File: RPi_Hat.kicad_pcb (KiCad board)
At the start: 2 copper layers, 65 x 56 mm, 50 parts, among them J1 Conn_01x02_Male, J2 RPi_GPIO, J3 Conn_02x03_Counter_Clockwise, J5 Conn_01x03_Male, J6 Conn_01x03_Male, J7 Conn_01x03_Male, J8 Conn_01x03_Male, J9 Conn_01x03_Male, SW1 SW_Push, U1 LM1085-5.0, U2 STM32F030CCTx, U3 MAX485E, U4 MAX485E, U5 MAX485E, U6 MAX485E, U7 MAX485E

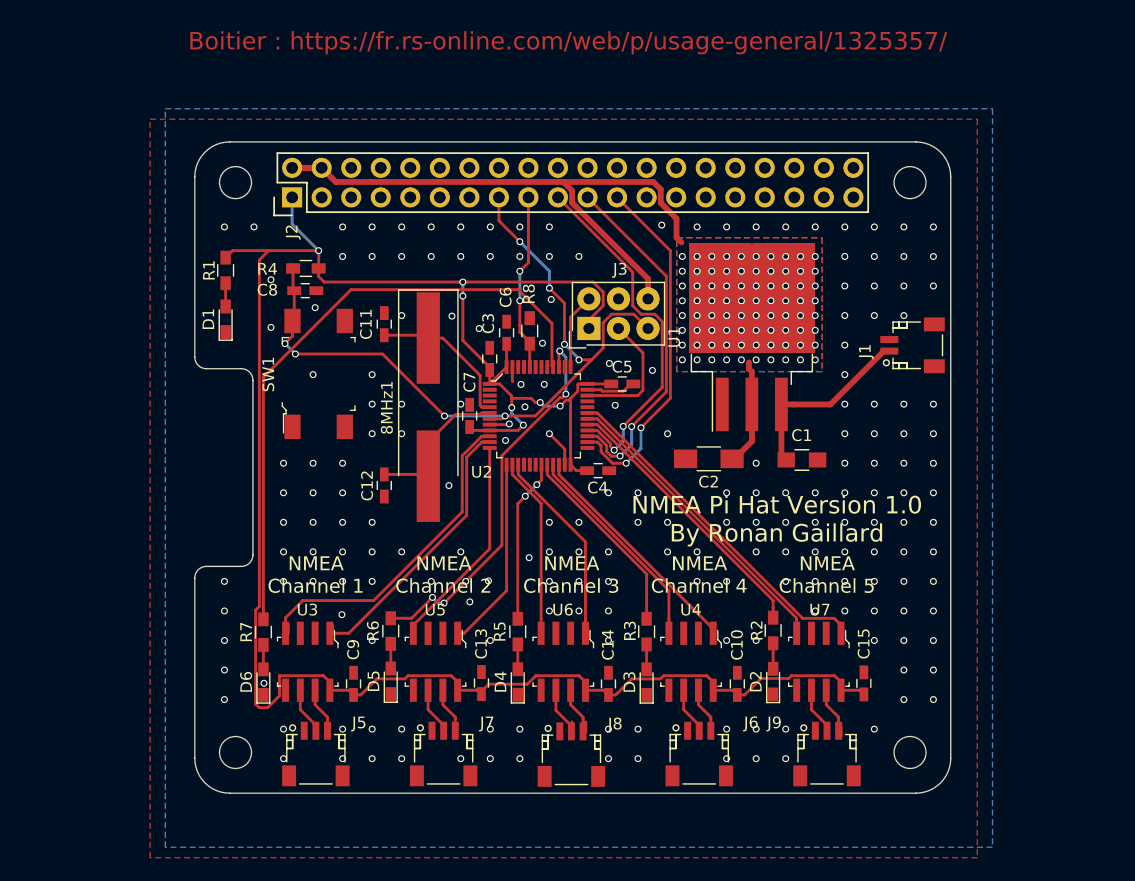
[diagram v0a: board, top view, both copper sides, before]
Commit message: Add terminaison resistors
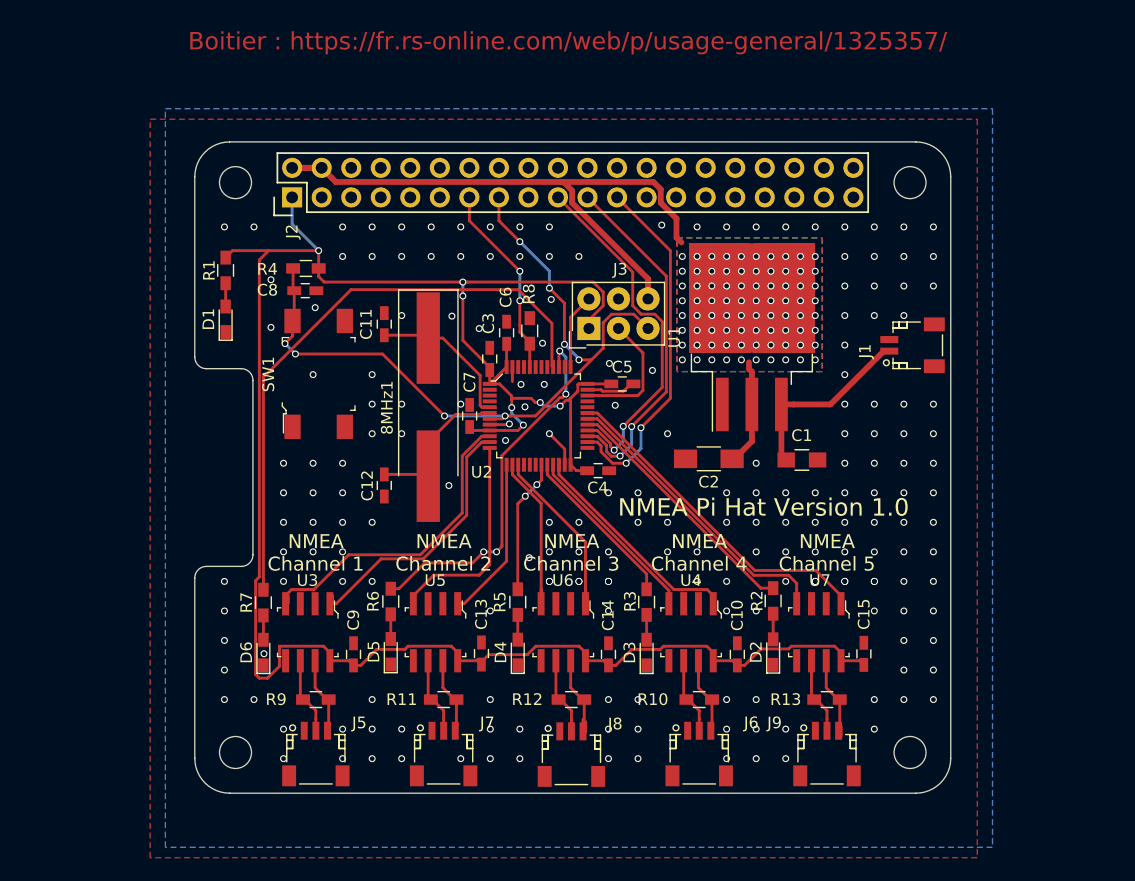
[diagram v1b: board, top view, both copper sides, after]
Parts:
- added R10: 120R, Resistors_SMD:R_0603_HandSoldering, F.Cu at (78.9, 76.2)
- added R11: 120R, Resistors_SMD:R_0603_HandSoldering, F.Cu at (56.9, 76.2)
- added R12: 120R, Resistors_SMD:R_0603_HandSoldering, F.Cu at (67.9, 76.2)
- added R13: 120R, Resistors_SMD:R_0603_HandSoldering, F.Cu at (89.9, 76.2)
- added R9: 120R, Resistors_SMD:R_0603_HandSoldering, F.Cu at (46.0, 76.2)
- moved C13 2.54 mm to (60.2, 72.2)
- moved C15 2.54 mm to (93.1, 72.3)
- moved D3 2.54 mm to (74.4, 72.2)
- moved D6 2.54 mm to (41.5, 72.2)
- moved R2 2.54 mm to (85.3, 67.7)
- moved R3 2.54 mm to (74.4, 67.8)
- moved R5 2.54 mm to (63.3, 67.8)
- moved R6 2.54 mm to (52.4, 67.8)
- moved R7 2.54 mm to (41.5, 67.9)
- moved U3 2.54 mm to (45.3, 70.4)
- moved U4 2.54 mm to (78.2, 70.4)
- moved U5 2.54 mm to (56.2, 70.4)
- moved U6 2.54 mm to (67.2, 70.4)
- moved U7 2.54 mm to (89.2, 70.4)
- moved C10 2.54 mm to (82.2, 72.3)
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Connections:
- J2 pad 13: Net-(J2-Pad13) -> /RPi_GPIO/BOOT0
- J2 pad 17: /RPi_GPIO/BOOT0 -> Net-(J2-Pad17)
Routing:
- net Net-(J6-Pad3): track 3.92 -> 7.88 mm
- net Net-(J8-Pad3): track 4.82 -> 8.56 mm
- net Net-(J8-Pad2): track 5.64 -> 8.74 mm
- net Net-(J6-Pad2): track 4.74 -> 7.84 mm
- net Net-(J7-Pad2): track 4.89 -> 7.99 mm
- net Net-(J5-Pad2): track 4.04 -> 7.14 mm
- net Net-(J9-Pad2): track 4.89 -> 7.99 mm
- net Net-(J9-Pad3): track 5.47 -> 8.18 mm
- net Net-(J5-Pad3): track 3.92 -> 6.63 mm
- net Net-(J7-Pad3): track 3.92 -> 6.63 mm
- net /RPi_GPIO/USART3_TX: track 18.6 -> 16.1 mm
- net /RPi_GPIO/USART2_RX: track 16.6 -> 14.0 mm
- net /RPi_GPIO/PB4: track 53.7 -> 51.2 mm
- net /RPi_GPIO/PB2: track 16.8 -> 14.2 mm
- net /RPi_GPIO/PB1: track 14.1 -> 11.6 mm
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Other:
- board text added: "NMEA Pi Hat Version 1.0"
- board text removed: "NMEA Pi Hat Version 1.0 By Ronan Gaillard"
